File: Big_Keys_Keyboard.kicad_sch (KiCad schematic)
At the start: 9 parts, among them U1 MX1A-11NN, U2 MX1A-11NN, U3 MX1A-11NN, U4 MX1A-11NN

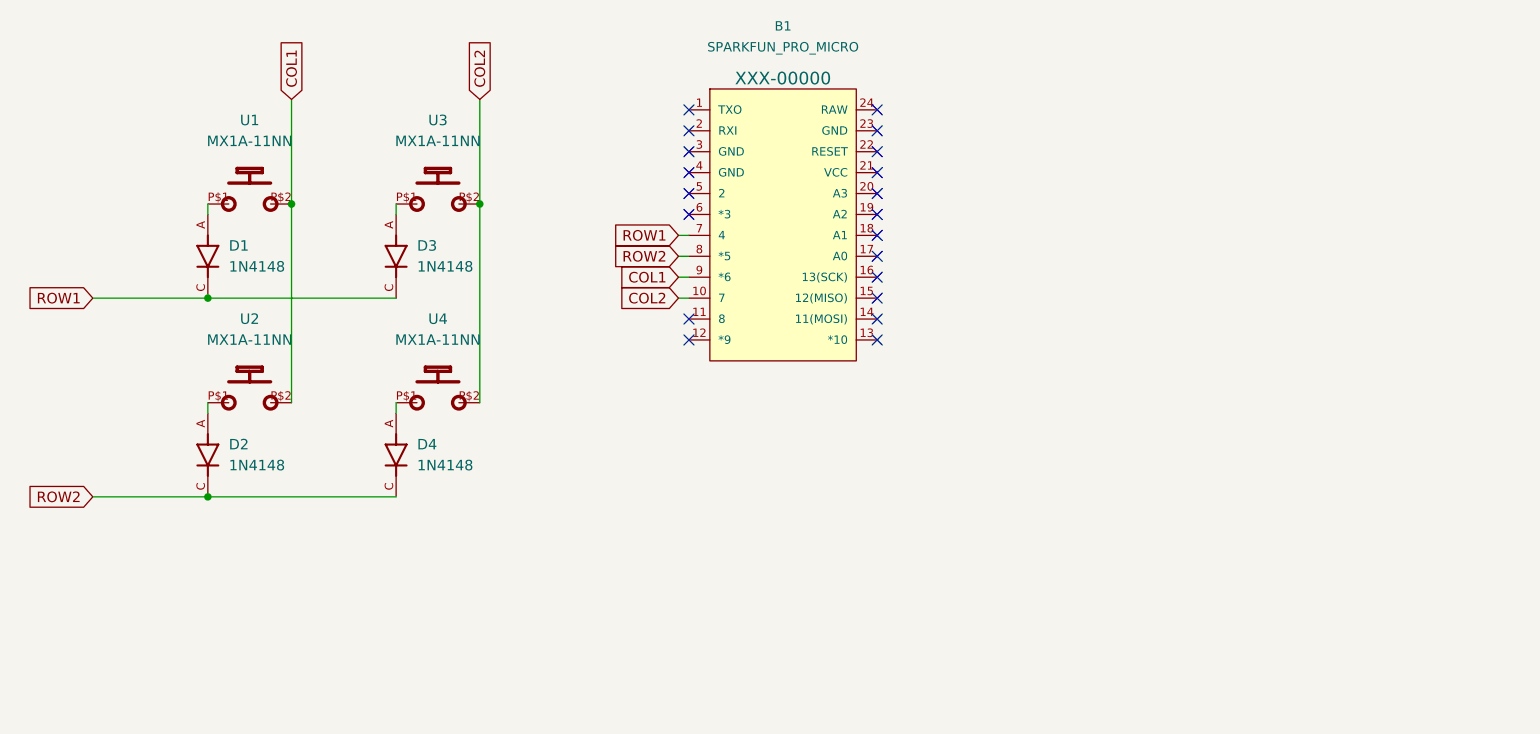
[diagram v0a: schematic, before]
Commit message: i2c bus with jst 4 pin ports on each side connected
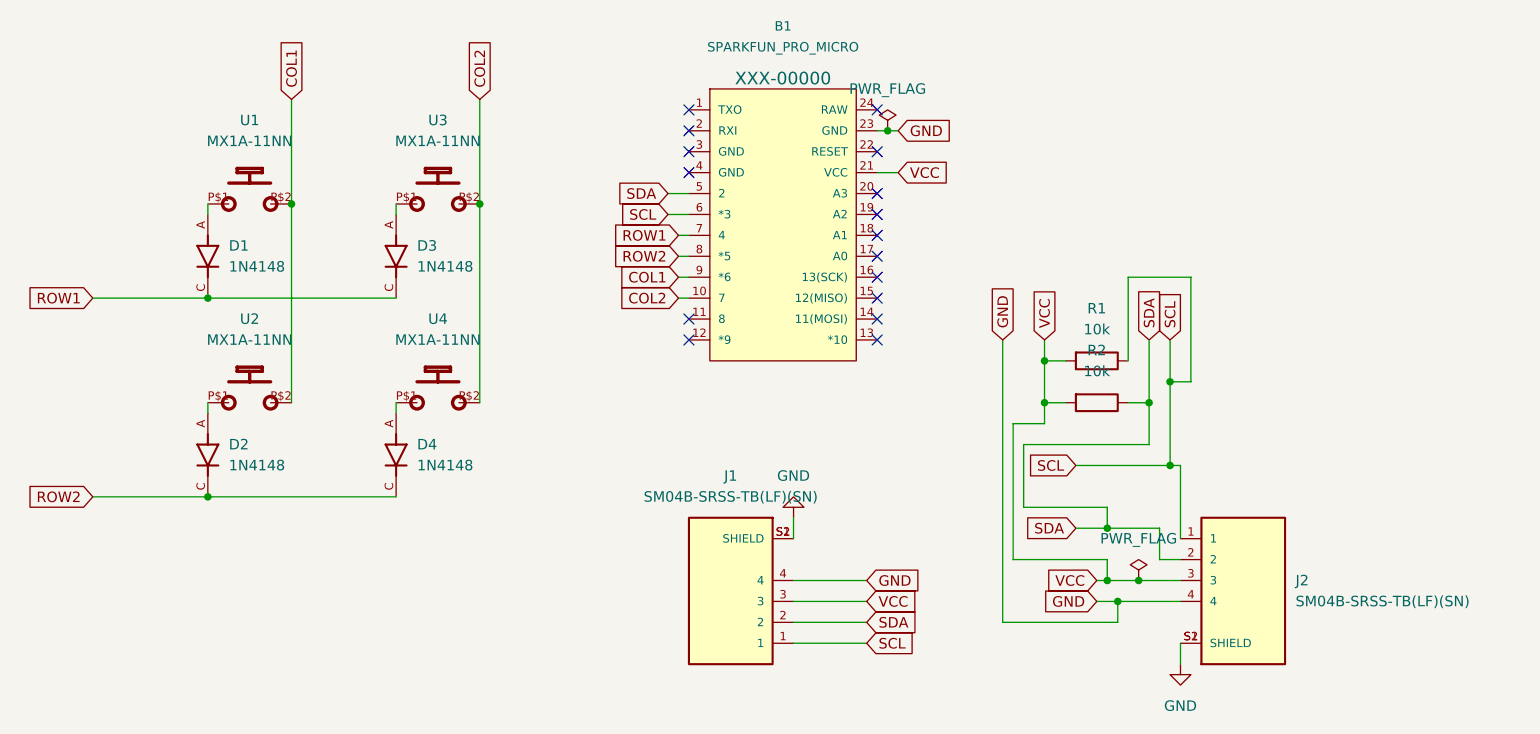
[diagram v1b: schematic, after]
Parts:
- added J1, J2: SM04B-SRSS-TB(LF)(SN), SM04B-SRSS-TB_LF__SN:JST_SM04B-SRSS-TB(LF)(SN), symbol SM04B-SRSS-TB_LF__SN_:SM04B-SRSS-TB(LF)(SN)
- added R1, R2: 10k, Resistor_THT:R_Axial_DIN0207_L6.3mm_D2.5mm_P10.16mm_Horizontal, symbol Device:R
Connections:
- net VCC: now reaches B1.21 (VCC)
- net VCC: now also J1.3, J2.3, R1.2, R2.2
- net GND: now reaches B1.23 (GND)
- net GND: now also J1.4, J1.S1 (SHIELD), J1.S2 (SHIELD), J2.4, J2.S1 (SHIELD), J2.S2 (SHIELD)
- net SDA: now reaches B1.5 (2)
- net SDA: now also J1.2, J2.2, R2.1
- net SCL: now reaches B1.6 (*3)
- net SCL: now also J1.1, J2.1, R1.1
- no-connect marks 20 -> 16

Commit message: printable design ready
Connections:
- net GND: now also B1.3 (GND), B1.4 (GND)
- no-connect marks 16 -> 14
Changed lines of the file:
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@@
   (no_connect (at 193.04 92.71))
   (no_connect (at 193.04 107.95))
-  (no_connect (at 170.18 87.63))
   (no_connect (at 193.04 102.87))
   (no_connect (at 170.18 82.55))
   (no_connect (at 170.18 85.09))
   (no_connect (at 193.04 100.33))
-  (no_connect (at 170.18 90.17))
   (no_connect (at 193.04 97.79))
   (no_connect (at 193.04 105.41))
@@
     (stroke (width 0) (type default) (color 0 0 0 0))
   )
+  (wire (pts (xy 167.64 87.63) (xy 170.18 87.63))
+    (stroke (width 0) (type default) (color 0 0 0 0))
+  )
   (wire (pts (xy 219.71 139.7) (xy 220.98 139.7))
     (stroke (width 0) (type default) (color 0 0 0 0))
@@
     (stroke (width 0) (type default) (color 0 0 0 0))
   )
+  (wire (pts (xy 167.64 90.17) (xy 170.18 90.17))
+    (stroke (width 0) (type default) (color 0 0 0 0))
+  )
   (wire (pts (xy 220.98 139.7) (xy 224.79 139.7))
     (stroke (width 0) (type default) (color 0 0 0 0))
@@
     )
   )
+  (global_label "GND" (shape input) (at 167.64 87.63 180) (fields_autoplaced)
+    (effects (font (size 1.27 1.27)) (justify right))
+    (property "Intersheet References" "${INTERSHEET_REFS}" (id 0) (at 161.3564 87.5506 0)
+      (effects (font (size 1.27 1.27)) (justify right) hide)
+    )
+  )
   (global_label "GND" (shape input) (at 219.71 142.24 180) (fields_autoplaced)
     (effects (font (size 1.27 1.27)) (justify right))
@@
       (effects (font (size 1.27 1.27)) (justify right) hide)
     )
+  )
+  (global_label "GND" (shape input) (at 167.64 90.17 180) (fields_autoplaced)
+    (effects (font (size 1.27 1.27)) (justify right))
+    (property "Intersheet References" "${INTERSHEET_REFS}" (id 0) (at 161.3564 90.0906 0)
+      (effects (font (size 1.27 1.27)) (justify right) hide)
+    )
